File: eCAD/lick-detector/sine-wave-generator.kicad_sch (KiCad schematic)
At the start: 18 parts, among them J7 J_PinHeader_01x02_2.54_V, J8 J_PinHeader_01x02_2.54_V, U3 OPA2365

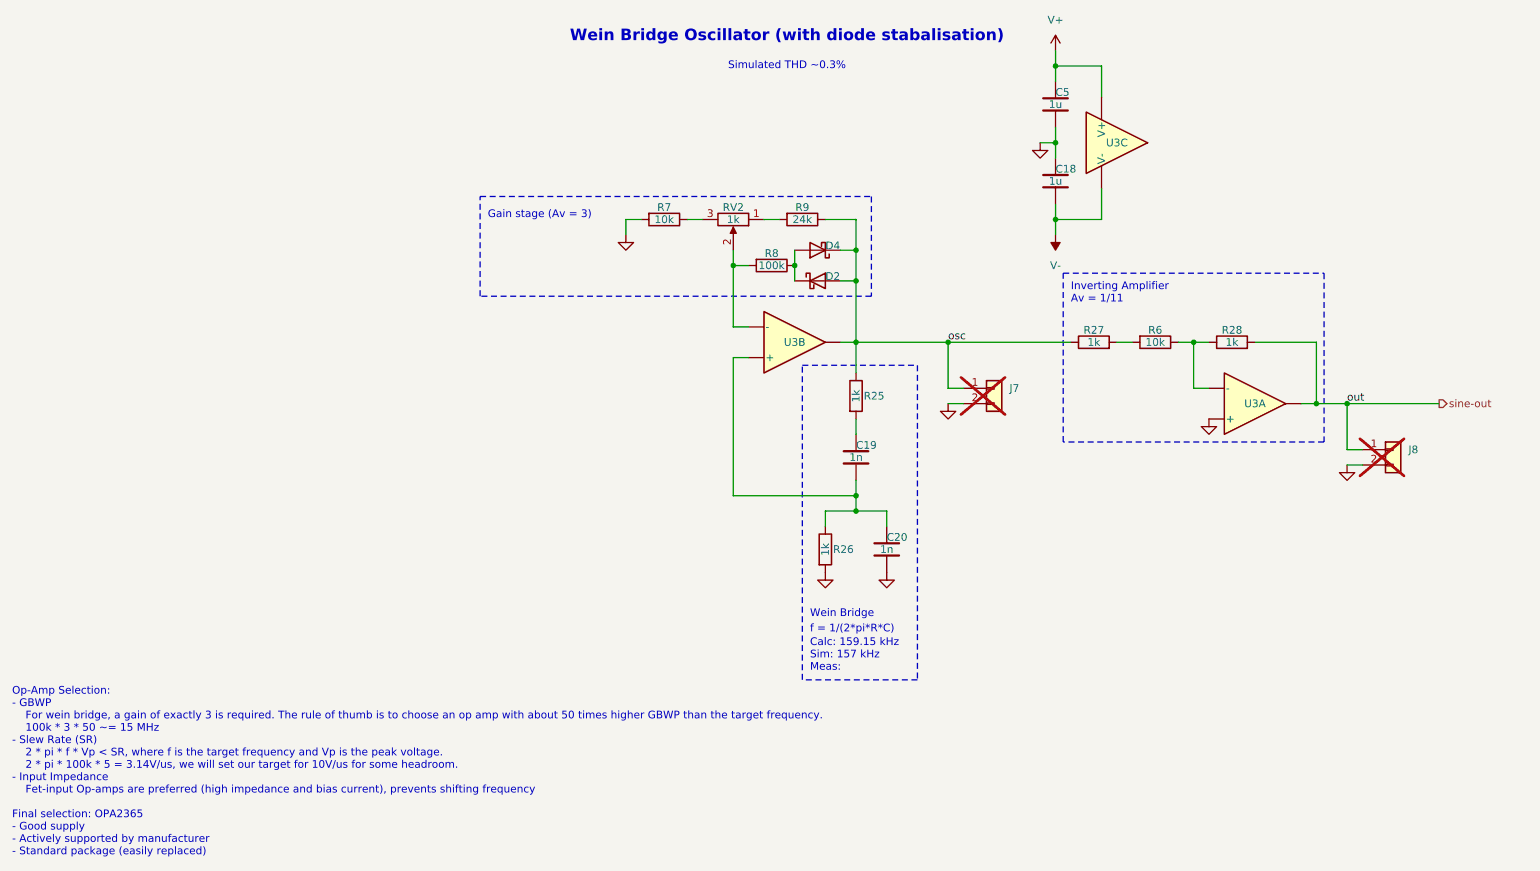
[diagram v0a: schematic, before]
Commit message: Number of upgrades complete: - Lower amplitude sine wave generator - Improved debug connector layout - Brightness of LED decreased - README updated with guide and areas for documentation - .gitignore added to ignore backup files and temporary files
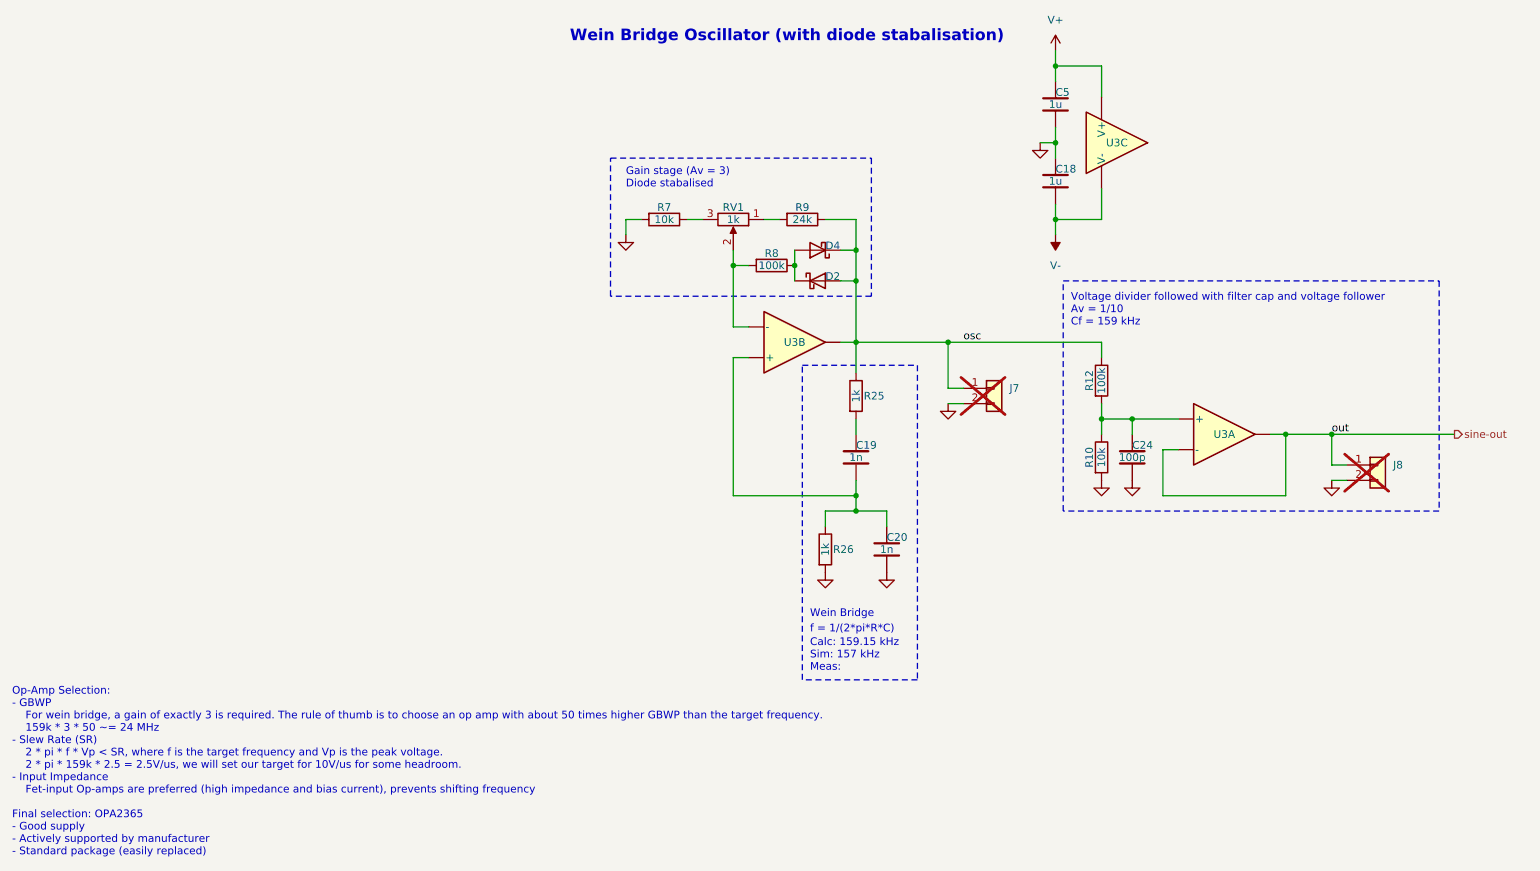
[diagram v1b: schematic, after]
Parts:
- removed R27, R28: 1k, !fablabs-kicad-library:R_0603_1608M, symbol !fablabs-kicad-library:R_0603_1k
- removed R6: 10k, !fablabs-kicad-library:R_0603_1608M, symbol !fablabs-kicad-library:R_0603_10k
- added C24: 100p, !fablabs-kicad-library:C_0603_1608M, symbol !fablabs-kicad-library:C_0603_100p_50V_C0G
- added R10: 10k, !fablabs-kicad-library:R_0603_1608M, symbol !fablabs-kicad-library:R_0603_10k
- added R12: 100k, !fablabs-kicad-library:R_0603_1608M, symbol !fablabs-kicad-library:R_0603_100k
- renumbered RV2 to RV1
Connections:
- net GND: now also C24.1, R10.1; no longer U3.3 (+)
- net osc: now also R12.2
- net sine-out: now also U3.2 (-)
- new net: C24.2, R10.2, R12.1, U3.3 (+)
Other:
- note added: "Gain stage (Av = 3) Diode stabalised"
- note added: "Op-Amp Selection: - GBWP For wein bridge, a gain of exactly 3 is required. The rule of thumb is to choose an op amp with about 50 times higher GBWP than the target frequency. 159k * 3 * 50 ~= 24 MHz - Slew Rate (SR) 2 * pi * f * Vp < SR, where f is the target frequency and Vp is the peak voltage. 2 * pi * 159k * 2.5 = 2.5V/us, we will set our target for 10V/us for some headroom. - Input Impedance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"
- note added: "Voltage divider followed with filter cap and voltage follower Av = 1/10 Cf = 159 kHz"
- note removed: "Gain stage (Av = 3)"
- note removed: "Inverting Amplifier Av = 1/11"
- note removed: "Op-Amp Selection: - GBWP For wein bridge, a gain of exactly 3 is required. The rule of thumb is to choose an op amp with about 50 times higher GBWP than the target frequency. 100k * 3 * 50 ~= 15 MHz - Slew Rate (SR) 2 * pi * f * Vp < SR, where f is the target frequency and Vp is the peak voltage. 2 * pi * 100k * 5 = 3.14V/us, we will set our target for 10V/us for some headroom. - Input Impedance 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"
- note removed: "Simulated THD ~0.3%"
- moved on the sheet: J8, U3A
